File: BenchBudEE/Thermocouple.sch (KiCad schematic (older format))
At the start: 0 parts

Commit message: Creating hierachical sheet connections.
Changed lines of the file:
@@
 Text HLabel 3650 3500 2    60   Input ~ 0
 TC IN-
+Text HLabel 1550 3350 0    60   Input ~ 0
+MOSI
+Text HLabel 1550 3500 0    60   Output ~ 0
+MISO
+Text HLabel 1550 3650 0    60   Input ~ 0
+SCLK
+Text HLabel 1550 3800 0    60   Input ~ 0
+CS_N
 $EndSCHEMATC

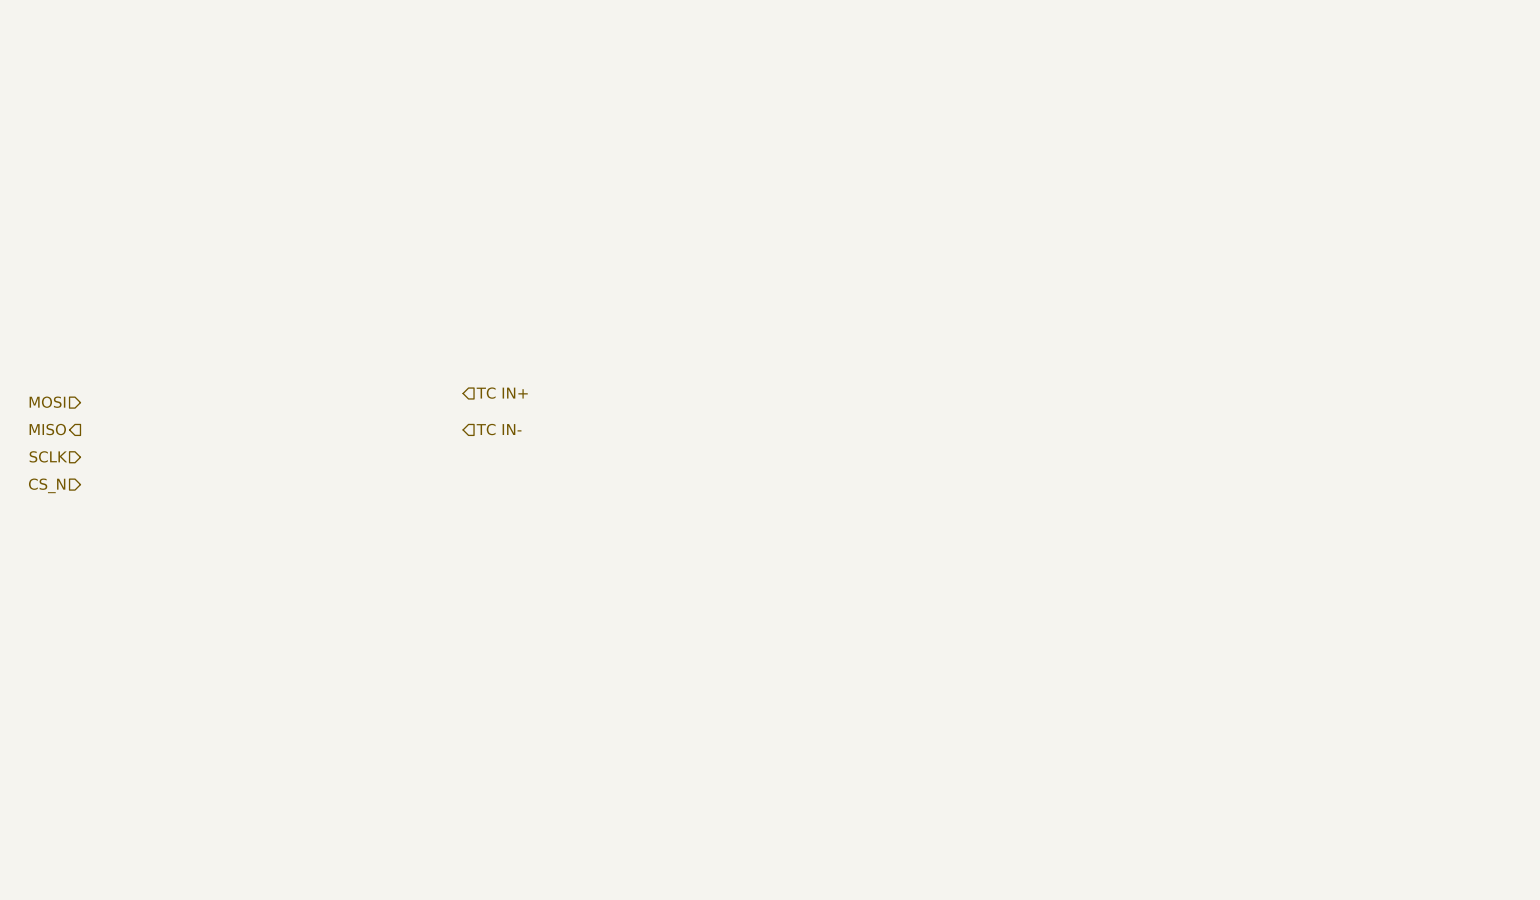
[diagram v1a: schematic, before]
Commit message: Implementing Thermocouple schematic
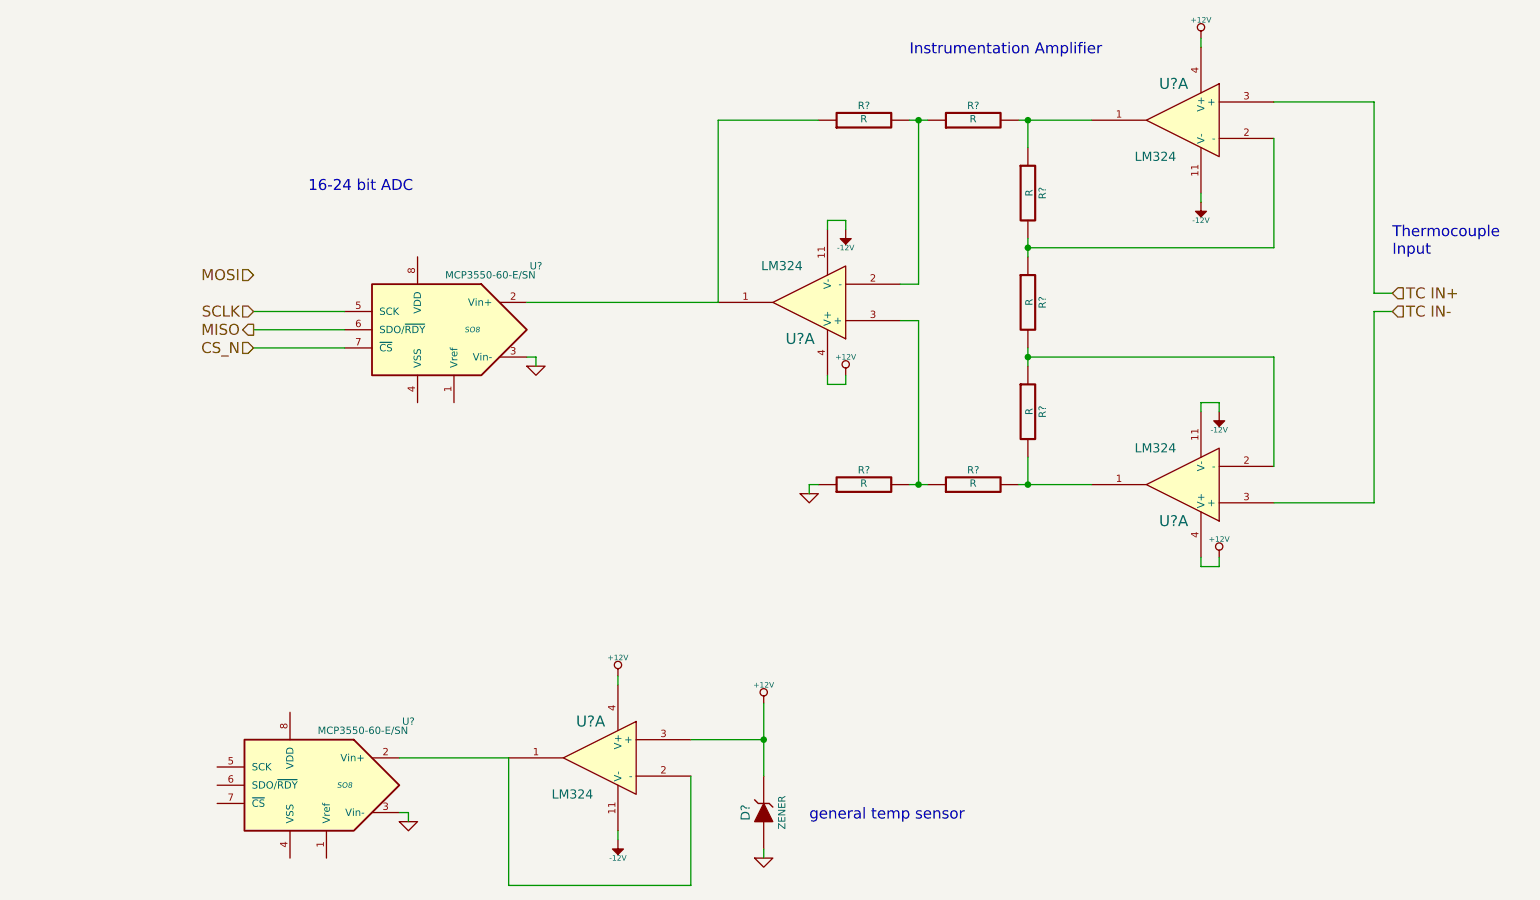
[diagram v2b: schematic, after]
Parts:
- added D?: ZENER, ~, symbol ZENER
- added R? (x7): R, ~, symbol R
- added U? (x4): LM324, symbol LM324
- added U? (x2): MCP3550-60-E/SN, SO8, symbol MCP3550-60-E/SN
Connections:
- net CS_N: now also U?.7 (~CS~)
- net MISO: now also U?.6 (SDO/~RDY~)
- net SCLK: now also U?.5 (SCK)
- net TC IN+: now also U?.3 (+)
- net TC IN-: now also U?.3 (+)
- new net: R?.1, R?.2, U?.1
- new net: R?.1, R?.2, U?.2 (-) (x3)
- new net: R?.2, R?.2, U?.1
- new net: R?.1, U?.1, U?.2 (Vin+)
- new net: R?.1, R?.2, U?.3 (+)
- new net: U?.1, U?.2 (-), U?.2 (Vin+)
- new net +12V: D?.2 (K), U?.3 (+), U?.4 (V+), U?.4 (V+), U?.4 (V+), U?.4 (V+)
- new net -12V: U?.11 (V-), U?.11 (V-), U?.11 (V-), U?.11 (V-)
- new net GND: D?.1 (A), R?.1, U?.3 (Vin-), U?.3 (Vin-)
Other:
- note added: "16-24 bit ADC"
- note added: "Instrumentation Amplifier"
- note added: "Thermocouple\nInput"
- note added: "general temp sensor"
